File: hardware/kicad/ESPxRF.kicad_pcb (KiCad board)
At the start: 4 copper layers, 67.6 x 28.7 mm, 36 parts, among them J1 USB_C_Receptacle_USB2.0, J2 ANT, U1 USBLC6-2SC6, U2 NCP115ASN330T2G, U3 ESP32-S3, U4 NRF24L01, Y1 Crystal_GND24_Small

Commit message: V2
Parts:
- removed L4: 2n7, Inductor_SMD:L_0402_1005Metric_Pad0.77x0.64mm_HandSolder
- added C18: 4p7, Capacitor_SMD:C_0402_1005Metric_Pad0.74x0.62mm_HandSolder, F.Cu at (146.1, 90.1)
- added C19: 100n, Capacitor_SMD:C_0603_1608Metric_Pad1.08x0.95mm_HandSolder, F.Cu at (146.4, 84.6)
- added C20: 1p5, Capacitor_SMD:C_0402_1005Metric_Pad0.74x0.62mm_HandSolder, F.Cu at (150.1, 87.0)
- added C21: 1p, Capacitor_SMD:C_0402_1005Metric_Pad0.74x0.62mm_HandSolder, F.Cu at (151.9, 87.6)
- added C4: 10u, Capacitor_SMD:C_0805_2012Metric_Pad1.18x1.45mm_HandSolder, F.Cu at (120.7, 100.7)
- C1, C5, C8: value 10u -> 100n
- C10, C13: value 100n -> 10u; footprint Capacitor_SMD:C_0402_1005Metric_Pad0.74x0.62mm_HandSolder -> Capacitor_SMD:C_0805_2012Metric_Pad1.18x1.45mm_HandSolder
- C11: value 22p -> 10u; footprint Capacitor_SMD:C_0402_1005Metric_Pad0.74x0.62mm_HandSolder -> Capacitor_SMD:C_0805_2012Metric_Pad1.18x1.45mm_HandSolder
- C12: value 2n2 -> 22p; footprint Capacitor_SMD:C_0402_1005Metric_Pad0.74x0.62mm_HandSolder -> Capacitor_SMD:C_0603_1608Metric_Pad1.08x0.95mm_HandSolder
- C14: value 4p7 -> 100n; footprint Capacitor_SMD:C_0402_1005Metric_Pad0.74x0.62mm_HandSolder -> Capacitor_SMD:C_0603_1608Metric_Pad1.08x0.95mm_HandSolder
- C15: value 100n -> 22p; footprint Capacitor_SMD:C_0402_1005Metric_Pad0.74x0.62mm_HandSolder -> Capacitor_SMD:C_0603_1608Metric_Pad1.08x0.95mm_HandSolder
- C16: value 1p5 -> 2n2
- C17: value 1p -> 100n; footprint Capacitor_SMD:C_0402_1005Metric_Pad0.74x0.62mm_HandSolder -> Capacitor_SMD:C_0603_1608Metric_Pad1.08x0.95mm_HandSolder
- C2: footprint Capacitor_SMD:C_0603_1608Metric_Pad1.08x0.95mm_HandSolder -> Capacitor_SMD:C_0805_2012Metric_Pad1.18x1.45mm_HandSolder
- C6: value 100n -> 10u; footprint Capacitor_SMD:C_0603_1608Metric_Pad1.08x0.95mm_HandSolder -> Capacitor_SMD:C_0805_2012Metric_Pad1.18x1.45mm_HandSolder
- C7: value 33n -> 10u; footprint Capacitor_SMD:C_0402_1005Metric_Pad0.74x0.62mm_HandSolder -> Capacitor_SMD:C_0805_2012Metric_Pad1.18x1.45mm_HandSolder
- C9: value 22p -> 33n; footprint Capacitor_SMD:C_0402_1005Metric_Pad0.74x0.62mm_HandSolder -> Capacitor_SMD:C_0603_1608Metric_Pad1.08x0.95mm_HandSolder
- J2: footprint Connector_Coaxial:SMA_Samtec_SMA-J-P-X-ST-EM1_EdgeMount -> Connector_Coaxial:SMA_Samtec_SMA-J-P-H-ST-EM1_EdgeMount
- L1: value 2u2 -> 8n2; footprint Inductor_SMD:L_0603_1608Metric_Pad1.05x0.95mm_HandSolder -> Inductor_SMD:L_0402_1005Metric_Pad0.77x0.64mm_HandSolder
- L2: value 8n2 -> 3n9
- L3: value 3n9 -> 2n7
- R1: value 5k1 -> 1k3
- R3: value 1k3 -> 5k1
- R5, R6: footprint Resistor_SMD:R_0402_1005Metric_Pad0.72x0.64mm_HandSolder -> Resistor_SMD:R_0603_1608Metric_Pad0.98x0.95mm_HandSolder
- U1: value USBLC6-2SC6 -> ESP32-S3; footprint Package_TO_SOT_SMD:SOT-23-6_Handsoldering -> ESP32-S3-WROOM:XCVR_ESP32S3WROOM1N8R8
- U2: value NCP115ASN330T2G -> USBLC6-2SC6; footprint Package_TO_SOT_SMD:SOT-23-5_HandSoldering -> Package_TO_SOT_SMD:SOT-23-6_Handsoldering
- U3: value ESP32-S3 -> NCP115ASN330T2G; footprint ESP32:XCVR_ESP32S3WROOM1N8R8 -> Package_TO_SOT_SMD:SOT-23-5_HandSoldering
- moved R2 64.5 mm to (139.5, 111.2), turned to 90 degrees
- moved J1 60.0 mm to (133.3, 114.3), turned to 0 degrees
- moved F1 56.4 mm to (136.5, 106.4), turned to -90 degrees
- moved C1 55.1 mm to (127.2, 114.7), turned to 90 degrees
- moved L1 52.6 mm to (146.1, 87.6), turned to -90 degrees
- moved C3 50.6 mm to (140.1, 106.4), turned to 90 degrees
- moved C2 50.5 mm to (138.3, 106.4), turned to 90 degrees
- moved C6 48.9 mm to (138.3, 102.5), turned to -90 degrees
- moved U2 48.0 mm to (132.9, 104.8), turned to 90 degrees
- moved U3 44.4 mm to (143.3, 104.3), turned to 90 degrees
- moved R3 44.2 mm to (127.2, 111.2), turned to 90 degrees
- moved R1 40.1 mm to (127.1, 100.6), turned to -90 degrees
- moved D1 39.5 mm to (127.1, 104.1), turned to 90 degrees
- moved D2 38.9 mm to (128.6, 104.1), turned to 90 degrees
- moved C5 35.9 mm to (120.5, 98.9), turned to 0 degrees
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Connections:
- C1 pad 1: +5V -> Net-(J1-SHIELD)
- C11 pad 1: XC2 -> +3V3
- C12 pad 1: VDD_PA -> XC1
- C14 pad 1: VDD_PA -> +3V3
- C15 pad 1: +3V3 -> XC2
- C16 pad 1: Net-(C16-Pad1) -> VDD_PA
- C16 pad 2: Net-(J2-In) -> GND
- C17 pad 1: Net-(J2-In) -> +3V3
- C2 pad 1: +3V3 -> +5V
- C3 pad 1: +3V3 -> +5V
- C7 pad 1: Net-(U4-DVDD) -> +3V3
- C9 pad 1: XC1 -> Net-(U4-DVDD)
- F1 pad 2: Net-(F1-Pad2) -> +5V
- J1 pad S1: unconnected-(J1-SHIELD-PadS1) -> Net-(J1-SHIELD)
- L1 pad 1: Net-(F1-Pad2) -> ANT2
- L1 pad 2: +5V -> ANT1
- L2 pad 2: ANT1 -> Net-(C20-Pad1)
- L3 pad 1: ANT2 -> ANT1
- L3 pad 2: Net-(C16-Pad1) -> VDD_PA
- R1 pad 1: Net-(J1-CC2) -> Net-(U1-IO16)
- R1 pad 2: GND -> Net-(D1-A)
- R2 pad 1: Net-(J1-CC1) -> Net-(J1-CC2)
- R3 pad 1: Net-(U3-IO16) -> Net-(J1-CC1)
- R3 pad 2: Net-(D1-A) -> GND
- R4 pad 1: Net-(U3-IO17) -> Net-(U1-IO17)
- U1 pad 1: USBCON_D- -> GND
- U1 pad 2: GND -> +3V3
- U1 pad 3: USBCON_D+ -> +3V3
- U1 pad 4: USB_D+ -> unconnected-(U1-IO4-Pad4)
- U1 pad 5: +5V -> unconnected-(U1-IO5-Pad5)
- U1 pad 6: USB_D- -> unconnected-(U1-IO6-Pad6)
- U2 pad 1: +5V -> USBCON_D-
- U2 pad 3: +5V -> USBCON_D+
- U2 pad 4: (no net) -> USB_D+
- U2 pad 5: +3V3 -> +5V
- U3 pad 1: GND -> +5V
- U3 pad 2: +3V3 -> GND
- U3 pad 3: +3V3 -> +5V
- U3 pad 4: unconnected-(U3-IO4-Pad4) -> (no net)
- U3 pad 5: unconnected-(U3-IO5-Pad5) -> +3V3
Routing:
- net +3V3: track 71.8 -> 37.9 mm, vias 4 -> 10
- net CSN: track 32.4 -> 5.27 mm, vias 2 -> 0
- net GND: track 84.0 -> 63.6 mm, vias 126 -> 31
- net MISO: track 24.2 -> 5.10 mm
- net Net-(J1-SHIELD): track 0.00 -> 18.9 mm
- net MOSI: track 22.0 -> 4.78 mm
- net SCK: track 19.5 -> 4.96 mm
- net +5V: track 14.2 -> 22.6 mm, vias 0 -> 2
- net Net-(U4-IREF): track 1.78 -> 9.41 mm, vias 0 -> 2
- net USB_D+: track 14.3 -> 6.81 mm
- net USB_D-: track 14.3 -> 6.81 mm
- net CE: track 12.6 -> 5.59 mm
- net IRQ: track 0.00 -> 6.18 mm
- net XC2: track 4.97 -> 9.60 mm
- net XC1: track 5.33 -> 9.79 mm
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- added copper zone on In2.Cu, net +3V3
- removed copper zone on In2.Cu, net GND
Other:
- board size 67.6 x 28.7 mm -> 42 x 49.9 mm
- board text removed: "ESP-RFLINK Thomas S. Perri GH: Tommy270502"
- board text removed: "JLCJLCJLCJLC"
- board text removed: "RX"
- board text removed: "TX"

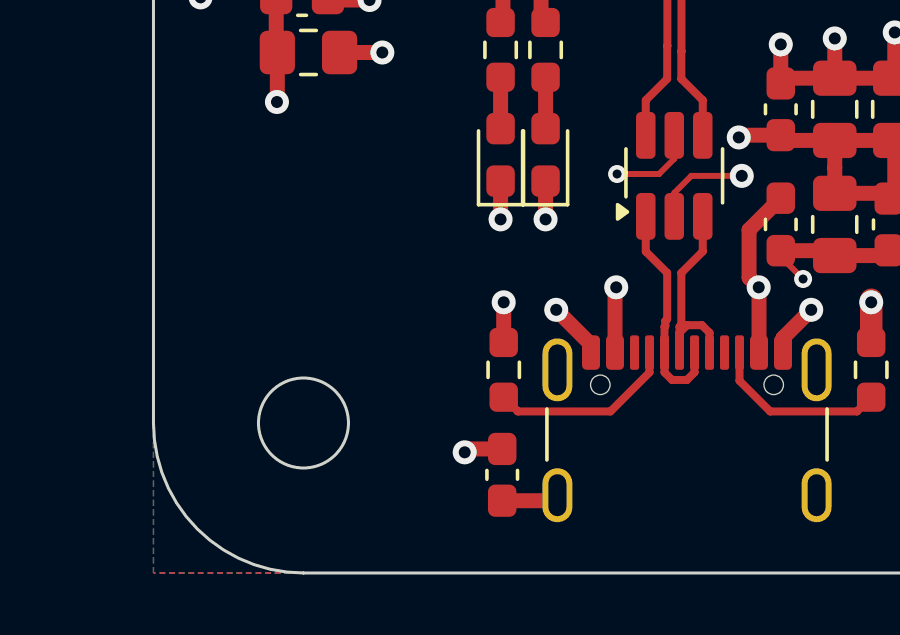
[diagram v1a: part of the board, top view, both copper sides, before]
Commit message: added keepout area for antenna and impedance matching network
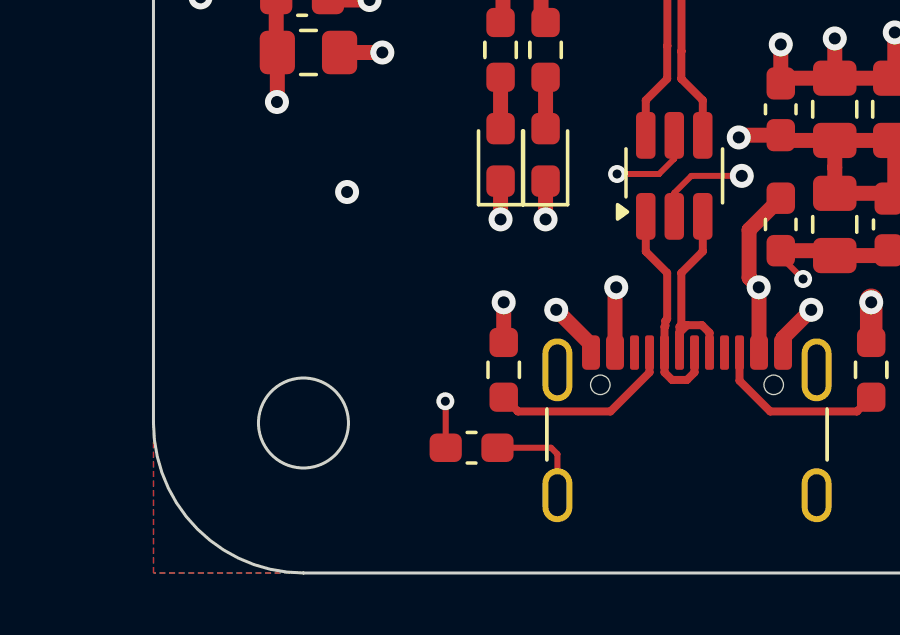
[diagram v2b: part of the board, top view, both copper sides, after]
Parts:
- moved C1 1.36 mm to (126.2, 113.8), turned to 180 degrees
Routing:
- net Net-(J1-SHIELD): track 18.9 -> 20.5 mm
- net GND: track 63.6 -> 63.8 mm, vias 31 -> 32
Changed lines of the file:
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@@
 	(footprint "Capacitor_SMD:C_0603_1608Metric_Pad1.08x0.95mm_HandSolder"
 		(layer "F.Cu")
-		(at 127.171046 114.727499 90)
+		(at 126.15 113.825 180)
 		(descr "Capacitor SMD 0603 (1608 Metric), square (rectangular) end terminal, IPC-7351 nominal with elongated pad for handsoldering. (Body size source: IPC-SM-782 page 76, https://www.pcb-3d.com/wordpress/wp-content/uploads/ipc-sm-782a_amendment_1_and_2.pdf), generated with kicad-footprint-generator")
 		(tags "capacitor handsolder")
 		(property "Reference" "C1"
-			(at 0 -1.43 90)
+			(at 0 -1.43 0)
 			(layer "F.SilkS")
 			(hide yes)
@@
 		)
 		(property "Value" "100n"
-			(at 0 1.43 90)
+			(at 0 1.43 0)
 			(layer "F.Fab")
 			(hide yes)
@@
 		)
 		(property "Datasheet" "~"
-			(at 0 0 90)
+			(at 0 0 0)
 			(layer "F.Fab")
 			(hide yes)
@@
 		)
 		(property "Description" ""
-			(at 0 0 90)
+			(at 0 0 0)
 			(layer "F.Fab")
 			(hide yes)
@@
 		(attr smd)
 		(fp_line
-			(start -0.146267 -0.51)
-			(end 0.146267 -0.51)
+			(start -0.146267 0.51)
+			(end 0.146267 0.51)
 			(stroke
 				(width 0.12)
@@
 		)
 		(fp_line
-			(start -0.146267 0.51)
-			(end 0.146267 0.51)
+			(start -0.146267 -0.51)
+			(end 0.146267 -0.51)
 			(stroke
 				(width 0.12)
@@
 		)
 		(fp_line
-			(start 1.65 -0.73)
-			(end 1.65 0.73)
+			(start 1.65 0.73)
+			(end -1.65 0.73)
 			(stroke
 				(width 0.05)
@@
 		)
 		(fp_line
-			(start -1.65 -0.73)
-			(end 1.65 -0.73)
+			(start 1.65 -0.73)
+			(end 1.65 0.73)
 			(stroke
 				(width 0.05)
@@
 		)
 		(fp_line
-			(start 1.65 0.73)
-			(end -1.65 0.73)
+			(start -1.65 0.73)
+			(end -1.65 -0.73)
 			(stroke
 				(width 0.05)
@@
 		)
 		(fp_line
-			(start -1.65 0.73)
-			(end -1.65 -0.73)
+			(start -1.65 -0.73)
+			(end 1.65 -0.73)
 			(stroke
 				(width 0.05)
@@
 		)
 		(fp_line
-			(start 0.8 -0.4)
-			(end 0.8 0.4)
+			(start 0.8 0.4)
+			(end -0.8 0.4)
 			(stroke
 				(width 0.1)
@@
 		)
 		(fp_line
-			(start -0.8 -0.4)
-			(end 0.8 -0.4)
+			(start 0.8 -0.4)
+			(end 0.8 0.4)
 			(stroke
 				(width 0.1)
@@
 		)
 		(fp_line
-			(start 0.8 0.4)
-			(end -0.8 0.4)
+			(start -0.8 0.4)
+			(end -0.8 -0.4)
 			(stroke
 				(width 0.1)
@@
 		)
 		(fp_line
-			(start -0.8 0.4)
-			(end -0.8 -0.4)
+			(start -0.8 -0.4)
+			(end 0.8 -0.4)
 			(stroke
 				(width 0.1)
@@
 		)
 		(fp_text user "${REFERENCE}"
-			(at 0 0 90)
+			(at 0 0 0)
 			(layer "F.Fab")
 			(effects
@@
 		)
 		(pad "1" smd roundrect
-			(at -0.8625 0 90)
+			(at -0.8625 0 180)
 			(size 1.075 0.95)
 			(layers "F.Cu" "F.Mask" "F.Paste")
@@
 		)
 		(pad "2" smd roundrect
-			(at 0.8625 0 90)
+			(at 0.8625 0 180)
 			(size 1.075 0.95)
 			(layers "F.Cu" "F.Mask" "F.Paste")
@@
 	)
 	(gr_rect
-		(start 115.546339 115.5)
-		(end 157.546339 118)
+		(start 154.546339 68.1)
+		(end 157.546339 118.040858)
 		(stroke
 			(width 0.15)
@@
 	)
 	(gr_rect
-		(start 154.546339 68.1)
+		(start 115.546339 115.040858)
 		(end 157.546339 118.040858)
 		(stroke
@@
 	)
 	(segment
+		(start 125.2875 112.2875)
+		(end 125.275 112.275)
+		(width 0.2032)
+		(layer "F.Cu")
+		(net 19)
+	)
+	(segment
 		(start 141.30363 98.902405)
 		(end 142.44375 100.042525)
@@
 	)
 	(segment
-		(start 117.03625 77.8925)
-		(end 117.11625 77.8125)
-		(width 0.5)
+		(start 125.2875 113.825)
+		(end 125.2875 112.2875)
+		(width 0.2032)
 		(layer "F.Cu")
 		(net 19)
 	)
 	(segment
-		(start 127.171046 113.864999)
-		(end 126.033546 113.864999)
+		(start 117.03625 77.8925)
+		(end 117.11625 77.8125)
 		(width 0.5)
 		(layer "F.Cu")
@@
 	)
 	(segment
-		(start 126.033546 113.864999)
-		(end 125.921046 113.977499)
-		(width 0.5)
-		(layer "F.Cu")
-		(net 19)
-	)
-	(segment
 		(start 139.88125 105.34375)
 		(end 140.05625 105.51875)
@@
 	)
 	(via
-		(at 125.921046 113.977499)
-		(size 0.8)
-		(drill 0.4)
-		(layers "F.Cu" "B.Cu")
-		(net 19)
-	)
-	(via
 		(at 148.94375 82.8125)
 		(size 0.8)
@@
 	)
 	(via
+		(at 122 105.3)
+		(size 0.8)
+		(drill 0.4)
+		(layers "F.Cu" "B.Cu")
+		(net 19)
+	)
+	(via
 		(at 117.11625 98.8125)
 		(size 0.8)
@@
 	)
 	(via
+		(at 125.275 112.275)
+		(size 0.6)
+		(drill 0.3)
+		(layers "F.Cu" "B.Cu")
+		(net 19)
+	)
+	(via
 		(at 117.11625 95.3125)
 		(size 0.8)
@@
 	)
 	(segment
-		(start 128.828546 115.589999)
+		(start 127.0125 113.825)
+		(end 128.8 113.825)
+		(width 0.2032)
+		(layer "F.Cu")
+		(net 29)
+	)
+	(segment
+		(start 129.011046 114.036046)
 		(end 129.011046 115.407499)
-		(width 0.5)
+		(width 0.2032)
 		(layer "F.Cu")
 		(net 29)
 	)
 	(segment
-		(start 127.171046 115.589999)
-		(end 128.828546 115.589999)
-		(width 0.5)
+		(start 128.8 113.825)
+		(end 129.011046 114.036046)
+		(width 0.2032)
 		(layer "F.Cu")
 		(net 29)
 	)
 	(segment
-		(start 129.011046 115.407499)
-		(end 129.011046 111.227499)
-		(width 0.5)
+		(start 137.651046 115.407499)
+		(end 129.011046 115.407499)
+		(width 0.2032)
 		(layer "In2.Cu")
 		(net 29)
 	)
 	(segment
-		(start 137.651046 115.407499)
-		(end 137.651046 111.227499)
-		(width 0.5)
+		(start 129.011046 111.227499)
+		(end 129.011046 115.407499)
+		(width 0.2032)
 		(layer "In2.Cu")
 		(net 29)
 	)
 	(segment
-		(start 129.011046 115.407499)
+		(start 137.651046 111.227499)
 		(end 137.651046 115.407499)
-		(width 0.5)
+		(width 0.2032)
 		(layer "In2.Cu")
 		(net 29)
@@
 			(thermal_gap 0.5)
 			(thermal_bridge_width 0.5)
+			(smoothing fillet)
+			(radius 1)
 		)
 		(polygon
